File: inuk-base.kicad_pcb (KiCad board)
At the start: 2 copper layers, 110 x 70 mm, 55 parts, among them J1 Conn_02x05_Odd_Even, J2 Conn_01x06, J3 Conn_01x02_Male, J4 Conn_01x02_Male, J5 Conn_01x08, Q1 DMG3406L, Q2 DMG3406L, Q3 DMG3406L, Q4 DMG3406L, Q5 DMG3406L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

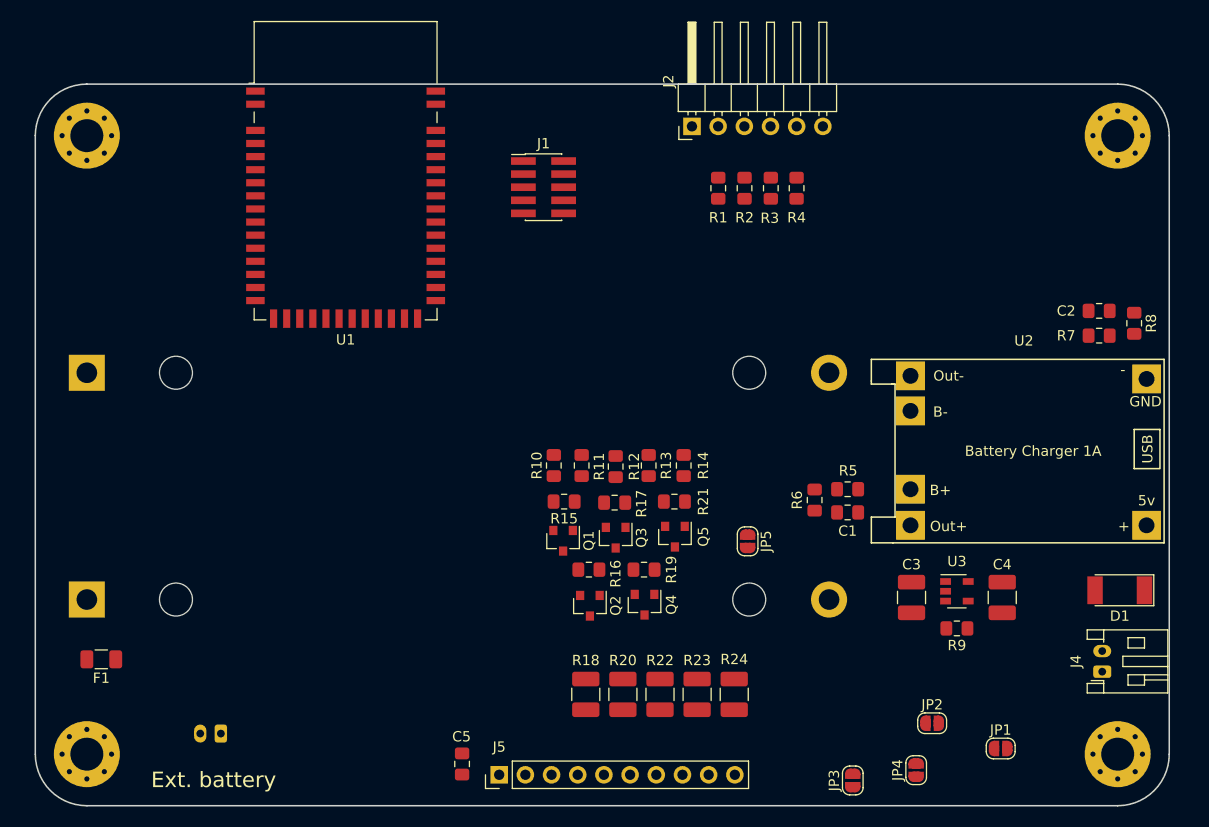
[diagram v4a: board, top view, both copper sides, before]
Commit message: added more circuit parts + new step files
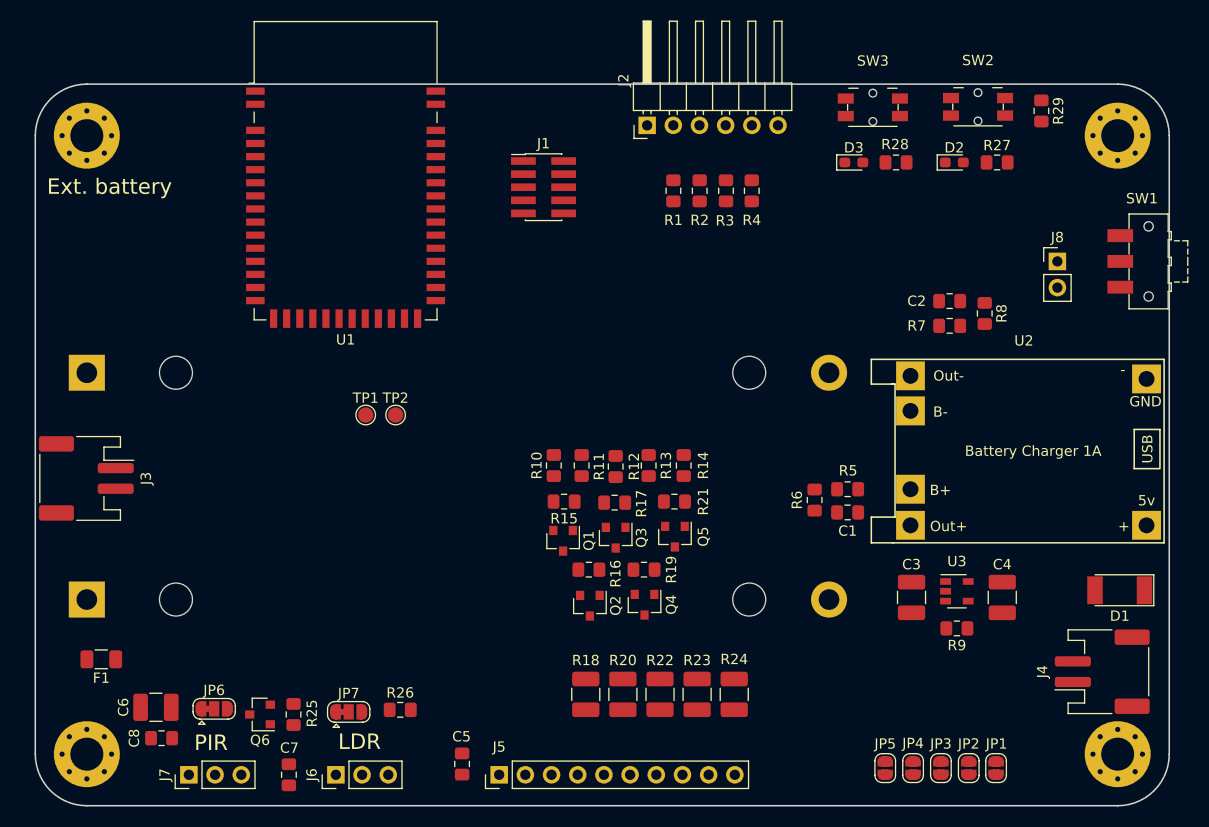
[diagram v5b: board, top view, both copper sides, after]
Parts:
- added C6: 10uF, Capacitor_SMD:C_1210_3225Metric_Pad1.42x2.65mm_HandSolder, F.Cu at (66.7, 135.4)
- added C7: 100nF, Capacitor_SMD:C_0805_2012Metric_Pad1.15x1.40mm_HandSolder, F.Cu at (79.6, 142.0)
- added C8: 100nF, Capacitor_SMD:C_0805_2012Metric_Pad1.15x1.40mm_HandSolder, F.Cu at (67.2, 138.4)
- added D2: LED, LED_SMD:LED_0603_1608Metric_Pad1.05x0.95mm_HandSolder, F.Cu at (144.2, 82.6)
- added D3: LED, LED_SMD:LED_0603_1608Metric_Pad1.05x0.95mm_HandSolder, F.Cu at (134.4, 82.6)
- added J6: Conn_01x03_Male, Connector_PinHeader_2.54mm:PinHeader_1x03_P2.54mm_Vertical, F.Cu at (84.2, 142.0)
- added J7: Conn_01x03_Male, Connector_PinHeader_2.54mm:PinHeader_1x03_P2.54mm_Vertical, F.Cu at (69.9, 142.0)
- added J8: Conn_01x02_Male, Connector_PinHeader_2.54mm:PinHeader_1x02_P2.54mm_Vertical, F.Cu at (154.2, 92.2)
- added JP6: SolderJumper_3_Bridged12, Jumper:SolderJumper-3_P1.3mm_Bridged12_RoundedPad1.0x1.5mm, F.Cu at (72.3, 135.6)
- added JP7: SolderJumper_3_Bridged12, Jumper:SolderJumper-3_P1.3mm_Bridged12_RoundedPad1.0x1.5mm, F.Cu at (85.4, 135.9)
- added Q6: BC817, Package_TO_SOT_SMD:SOT-23, F.Cu at (76.8, 136.2)
- added R25: 1k, Resistor_SMD:R_0805_2012Metric_Pad1.15x1.40mm_HandSolder, F.Cu at (80.0, 136.2)
- added R26: 100k, Resistor_SMD:R_0805_2012Metric_Pad1.15x1.40mm_HandSolder, F.Cu at (90.4, 135.7)
- added R27: 1K, Resistor_SMD:R_0805_2012Metric_Pad1.15x1.40mm_HandSolder, F.Cu at (148.3, 82.6)
- added R28: 1K, Resistor_SMD:R_0805_2012Metric_Pad1.15x1.40mm_HandSolder, F.Cu at (138.5, 82.6)
- added R29: 100k, Resistor_SMD:R_0805_2012Metric_Pad1.15x1.40mm_HandSolder, F.Cu at (152.6, 77.6)
- added SW1: SW_Push_SPDT, Button_Switch_SMD:SW_SPDT_CK-JS102011SAQN, F.Cu at (163.0, 92.2)
- added SW2: SW_Push, Button_Switch_SMD:Panasonic_EVQPUL_EVQPUC, F.Cu at (146.4, 77.2)
- added SW3: SW_Push, Button_Switch_SMD:Panasonic_EVQPUL_EVQPUC, F.Cu at (136.2, 77.2)
- added TP1: TestPoint, TestPoint:TestPoint_Pad_D1.5mm, F.Cu at (87.0, 107.1)
- added TP2: TestPoint, TestPoint:TestPoint_Pad_D1.5mm, F.Cu at (90.0, 107.1)
- J3: footprint Connector_JST:JST_PH_S2B-PH-K_1x02_P2.00mm_Horizontal -> Connector_JST:JST_PH_S2B-PH-SM4-TB_1x02-1MP_P2.00mm_Horizontal; moved to F.Cu
- J4: footprint Connector_JST:JST_PH_S2B-PH-K_1x02_P2.00mm_Horizontal -> Connector_JST:JST_PH_S2B-PH-SM4-TB_1x02-1MP_P2.00mm_Horizontal
- moved J3 28.0 mm to (60.0, 113.2), turned to 270 degrees
- moved JP5 25.7 mm to (137.4, 141.3)
- moved C2 14.5 mm to (143.7, 96.0)
- moved R7 14.5 mm to (143.7, 98.5)
- moved R8 14.5 mm to (147.1, 97.2)
- moved JP3 8.63 mm to (142.8, 141.3)
- moved JP2 5.61 mm to (145.6, 141.3), turned to 90 degrees
- moved R1 4.36 mm to (116.9, 85.3)
- moved R2 4.36 mm to (119.5, 85.3)
- moved R3 4.36 mm to (122.0, 85.3)
- moved R4 4.36 mm to (124.5, 85.3)
- moved J2 4.35 mm to (114.3, 79.0)
- moved JP1 1.95 mm to (148.2, 141.3), turned to 90 degrees
- moved JP4 0.36 mm to (140.2, 141.3)
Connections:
- net Net-(U1-Pad10) renamed /cpu/ain6
- net Net-(U1-Pad11) renamed /cpu/ain7
- net Net-(U1-Pad8) renamed /cpu/ain4
- net Net-(U1-Pad9) renamed /cpu/ain5
- C3 pad 1: Net-(C3-Pad1) -> /power/VIN
- J3 pad 1: +BATT -> GND
- J3 pad 2: GND -> +BATT
- J4 pad 1: Net-(D1-Pad2) -> GND
- J4 pad 2: GND -> Net-(D1-Pad2)
- J5 pad 2: /light_ctrl/sense -> /cpu/ain2
- R10 pad 2: /light_ctrl/lio_1 -> /cpu/lio1
- R11 pad 2: /light_ctrl/lio_2 -> /cpu/lio2
- R12 pad 2: /light_ctrl/lio_3 -> /cpu/lio3
- R13 pad 2: /light_ctrl/lio_4 -> /cpu/lio4
- R14 pad 2: /light_ctrl/lio_5 -> /cpu/lio5
- R9 pad 1: Net-(C3-Pad1) -> /power/EN
- R9 pad 2: Net-(R9-Pad2) -> GND
- U1 pad 17: /cpu/P0.02 -> /power/VBAT_ADC
- U1 pad 18: /cpu/P0.03 -> /power/VSOLAR_ADC
- U1 pad 19: /cpu/P0.04 -> /cpu/ain2
- U1 pad 20: /cpu/uart_cts -> /cpu/ain3
- U1 pad 26: /cpu/P0.11 -> /cpu/lio1
- U1 pad 27: /cpu/P0.12 -> /cpu/lio2
- U1 pad 28: /cpu/P0.13 -> /cpu/lio3
- U1 pad 29: /cpu/P0.14 -> /cpu/lio4
- U1 pad 30: /cpu/P0.15 -> /cpu/lio5
- U1 pad 31: /cpu/P0.16 -> /cpu/pir_input
- U2 pad 3: Net-(C3-Pad1) -> /power/VIN
- U3 pad 1: Net-(C3-Pad1) -> /power/VIN
- U3 pad 3: Net-(R9-Pad2) -> /power/EN
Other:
- board text added: "LDR"
- board text added: "PIR"

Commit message: started pcb routing
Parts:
- added U4: Logo_NM, Custom:Logo_NM, F.Cu at (153.1, 141.1)
- J3, JP1, JP2, JP3, JP4, JP5: moved to B.Cu
- moved J3 85.5 mm to (141.2, 140.0), turned to 180 degrees
- moved F1 73.9 mm to (133.4, 114.2)
- moved BT1 72.0 mm to (132.0, 103.8), turned to 180 degrees
- moved BT2 72.0 mm to (132.0, 125.5), turned to 180 degrees
- moved JP1 37.0 mm to (111.3, 139.0), turned to 270 degrees
- moved R9 35.8 mm to (145.5, 92.0), turned to 0 degrees
- moved JP2 31.5 mm to (114.1, 139.0), turned to 270 degrees
- moved C4 30.9 mm to (139.1, 95.5), turned to 90 degrees
- moved C3 29.9 mm to (147.2, 95.8), turned to 90 degrees
- moved U3 28.7 mm to (143.2, 95.5), turned to 180 degrees
- moved R8 26.4 mm to (123.7, 109.4)
- moved JP3 26.1 mm to (116.9, 139.0), turned to 270 degrees
- moved C2 22.1 mm to (126.9, 110.5), turned to 0 degrees
- moved JP4 20.6 mm to (119.7, 139.0), turned to 270 degrees
- moved R7 19.5 mm to (126.9, 108.3), turned to 180 degrees
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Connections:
- net Net-(J2-Pad2) renamed /uart/tx
- net Net-(J2-Pad3) renamed /uart/rx
- net Net-(J2-Pad4) renamed /uart/rts
- net Net-(J2-Pad5) renamed /uart/cts
- J6 pad 2: /cpu/ain3 -> /pir/ldr_sense
- R26 pad 1: /cpu/ain3 -> /pir/ldr_sense
- U1 pad 20: /cpu/ain3 -> /cpu/uart_rts
- U1 pad 21: /cpu/uart_rx -> /cpu/uart_tx
- U1 pad 22: /cpu/uart_rts -> /cpu/uart_cts
- U1 pad 23: /cpu/uart_tx -> /cpu/uart_rx
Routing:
- net +BATT: track 0.00 -> 80.9 mm, vias 0 -> 1
- net GND: track 0.00 -> 65.1 mm, vias 0 -> 13
- net /power/VIN: track 0.00 -> 42.6 mm, vias 0 -> 1
- net /cpu/lio5: track 0.00 -> 36.5 mm
- net /cpu/lio4: track 0.00 -> 32.9 mm
- net /cpu/lio3: track 0.00 -> 29.4 mm
- net /light_ctrl/lio_1_sig: track 0.00 -> 28.3 mm, vias 0 -> 1
- net /light_ctrl/lio_2_sig: track 0.00 -> 25.8 mm, vias 0 -> 1
- net /cpu/lio2: track 0.00 -> 25.5 mm
- net /cpu/pir_input: track 0.00 -> 23.8 mm
- net /cpu/lio1: track 0.00 -> 23.7 mm
- net /light_ctrl/lio_3_sig: track 0.00 -> 23.7 mm, vias 0 -> 1
- net /power/EN: track 0.00 -> 22.1 mm
- net /cpu/nRESET: track 0.00 -> 21.8 mm
- net Net-(BT1-Pad1): track 0.00 -> 21.7 mm
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- added copper zone on F.Cu, net +3V3
- added copper zone on F.Cu, net /power/VIN
- added copper zone on B.Cu, net GND
- added copper zone on F.Cu, net GND
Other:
- board text added: "3V3"
- board text added: "AIN"
- board text added: "CTS"
- board text added: "ENABLE"
- board text added: "GND"
- board text added: "IN"
- board text added: "LIGHT"
- board text added: "LIO1"
- board text added: "LIO2"
- board text added: "LIO3"
- board text added: "LIO4"
- board text added: "LIO5"
- board text added: "OFF"
- board text added: "ON"
- board text added: "P0.25"
- board text added: "P0.26"
- board text added: "P0.27"
- board text added: "RESET"
- board text added: "RTS"
- board text added: "RX"
- board text added: "SOLAR"
- board text added: "SWCLK"
- board text added: "SWDIO"
- board text added: "SWO"
- board text added: "TX"
- board text added: "VBAT"
- board text added: "VCC"
- board text added: "VIN"
- board text removed: "Ext. battery"

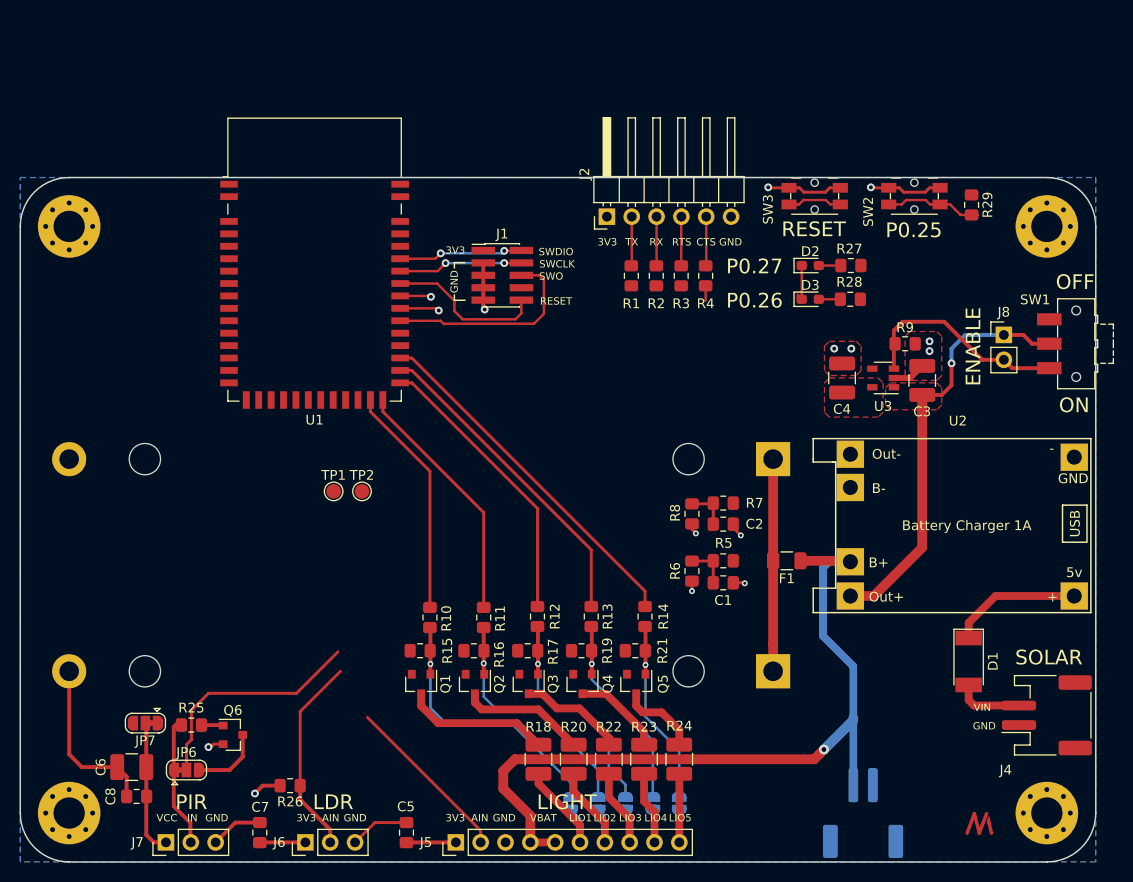
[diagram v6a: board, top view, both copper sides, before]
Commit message: more layout + resized pcb to 100 x 80
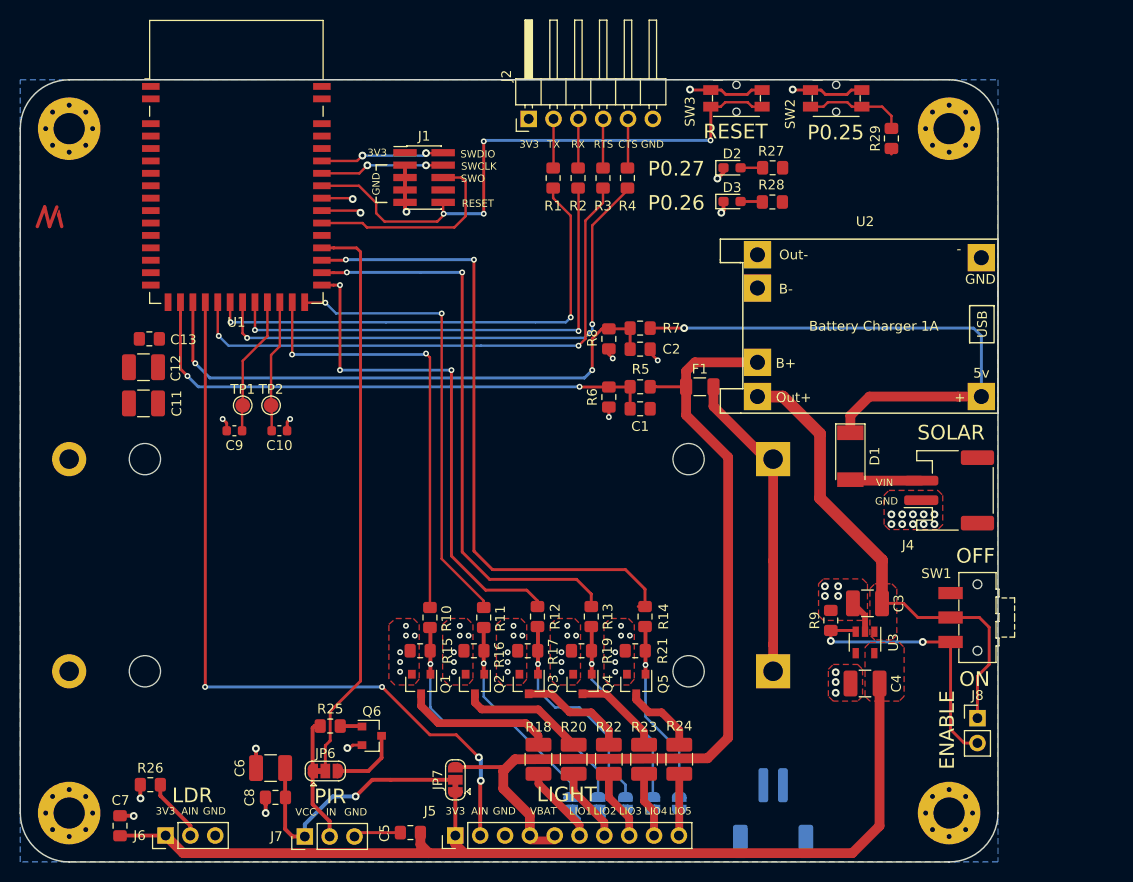
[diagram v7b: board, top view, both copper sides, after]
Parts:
- added C10: NC, Capacitor_SMD:C_0603_1608Metric, F.Cu at (81.5, 100.9)
- added C11: 10uF, Capacitor_SMD:C_1210_3225Metric_Pad1.42x2.65mm_HandSolder, F.Cu at (67.6, 98.1)
- added C12: 10uF, Capacitor_SMD:C_1210_3225Metric_Pad1.42x2.65mm_HandSolder, F.Cu at (67.6, 94.4)
- added C13: 100nF, Capacitor_SMD:C_0805_2012Metric_Pad1.15x1.40mm_HandSolder, F.Cu at (68.2, 91.5)
- added C9: NC, Capacitor_SMD:C_0603_1608Metric, F.Cu at (76.9, 100.9)
- moved U4 113.6 mm to (58.0, 79.0)
- moved J8 39.3 mm to (152.9, 130.3)
- moved JP7 32.2 mm to (99.5, 136.6), turned to 90 degrees
- moved C4 31.3 mm to (141.4, 126.8), turned to 180 degrees
- moved SW1 29.8 mm to (152.9, 120.0)
- moved R9 29.3 mm to (137.9, 120.3), turned to 90 degrees
- moved U3 27.1 mm to (141.4, 122.5), turned to 270 degrees
- moved J4 25.1 mm to (150.0, 107.0)
- moved D1 24.2 mm to (139.9, 103.5)
- moved C3 23.5 mm to (141.7, 118.5), turned to 180 degrees
- moved U2 22.5 mm to (155.0, 99.1)
- moved F1 19.9 mm to (124.5, 96.4), turned to 0 degrees
- moved C2 19.8 mm to (118.4, 92.5)
- moved R8 19.8 mm to (115.2, 91.5)
- moved R7 19.8 mm to (118.4, 90.4)
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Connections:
- net Net-(U1-Pad12) renamed /cpu/DEC4
- net Net-(U1-Pad13) renamed /cpu/DCC
- U1 pad 16: Net-(U1-Pad16) -> +3V3
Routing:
- net +3V3: track 9.73 -> 104.9 mm
- net /cpu/ain2: track 17.6 -> 78.5 mm, vias 0 -> 4
- net /cpu/uart_rts: track 0.00 -> 57.9 mm, vias 0 -> 2
- net /cpu/uart_cts: track 1.52 -> 55.5 mm, vias 0 -> 2
- net /power/VSOLAR_ADC: track 4.36 -> 57.6 mm, vias 0 -> 2
- net /power/VBAT_ADC: track 4.44 -> 55.8 mm, vias 0 -> 2
- net /cpu/uart_tx: track 0.00 -> 51.0 mm, vias 0 -> 2
- net /cpu/uart_rx: track 0.00 -> 50.6 mm, vias 0 -> 2
- net /power/VSOLAR: track 13.5 -> 56.4 mm, vias 0 -> 1
- net /cpu/nRESET: track 21.8 -> 60.0 mm, vias 0 -> 4
- net /cpu/pir_input: track 23.8 -> 58.7 mm
- net /cpu/lio5: track 36.5 -> 67.0 mm, vias 0 -> 2
- net /cpu/lio4: track 32.9 -> 59.2 mm, vias 0 -> 2
- net /cpu/lio3: track 29.4 -> 52.2 mm, vias 0 -> 3
- net /cpu/lio1: track 23.7 -> 45.2 mm, vias 0 -> 2
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- added copper zone on F.Cu, net (none)
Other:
- board size 110 x 70 mm -> 100 x 80 mm
